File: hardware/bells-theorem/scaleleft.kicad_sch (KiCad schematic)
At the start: 30 parts, among them U20 TL074, U21 TL072

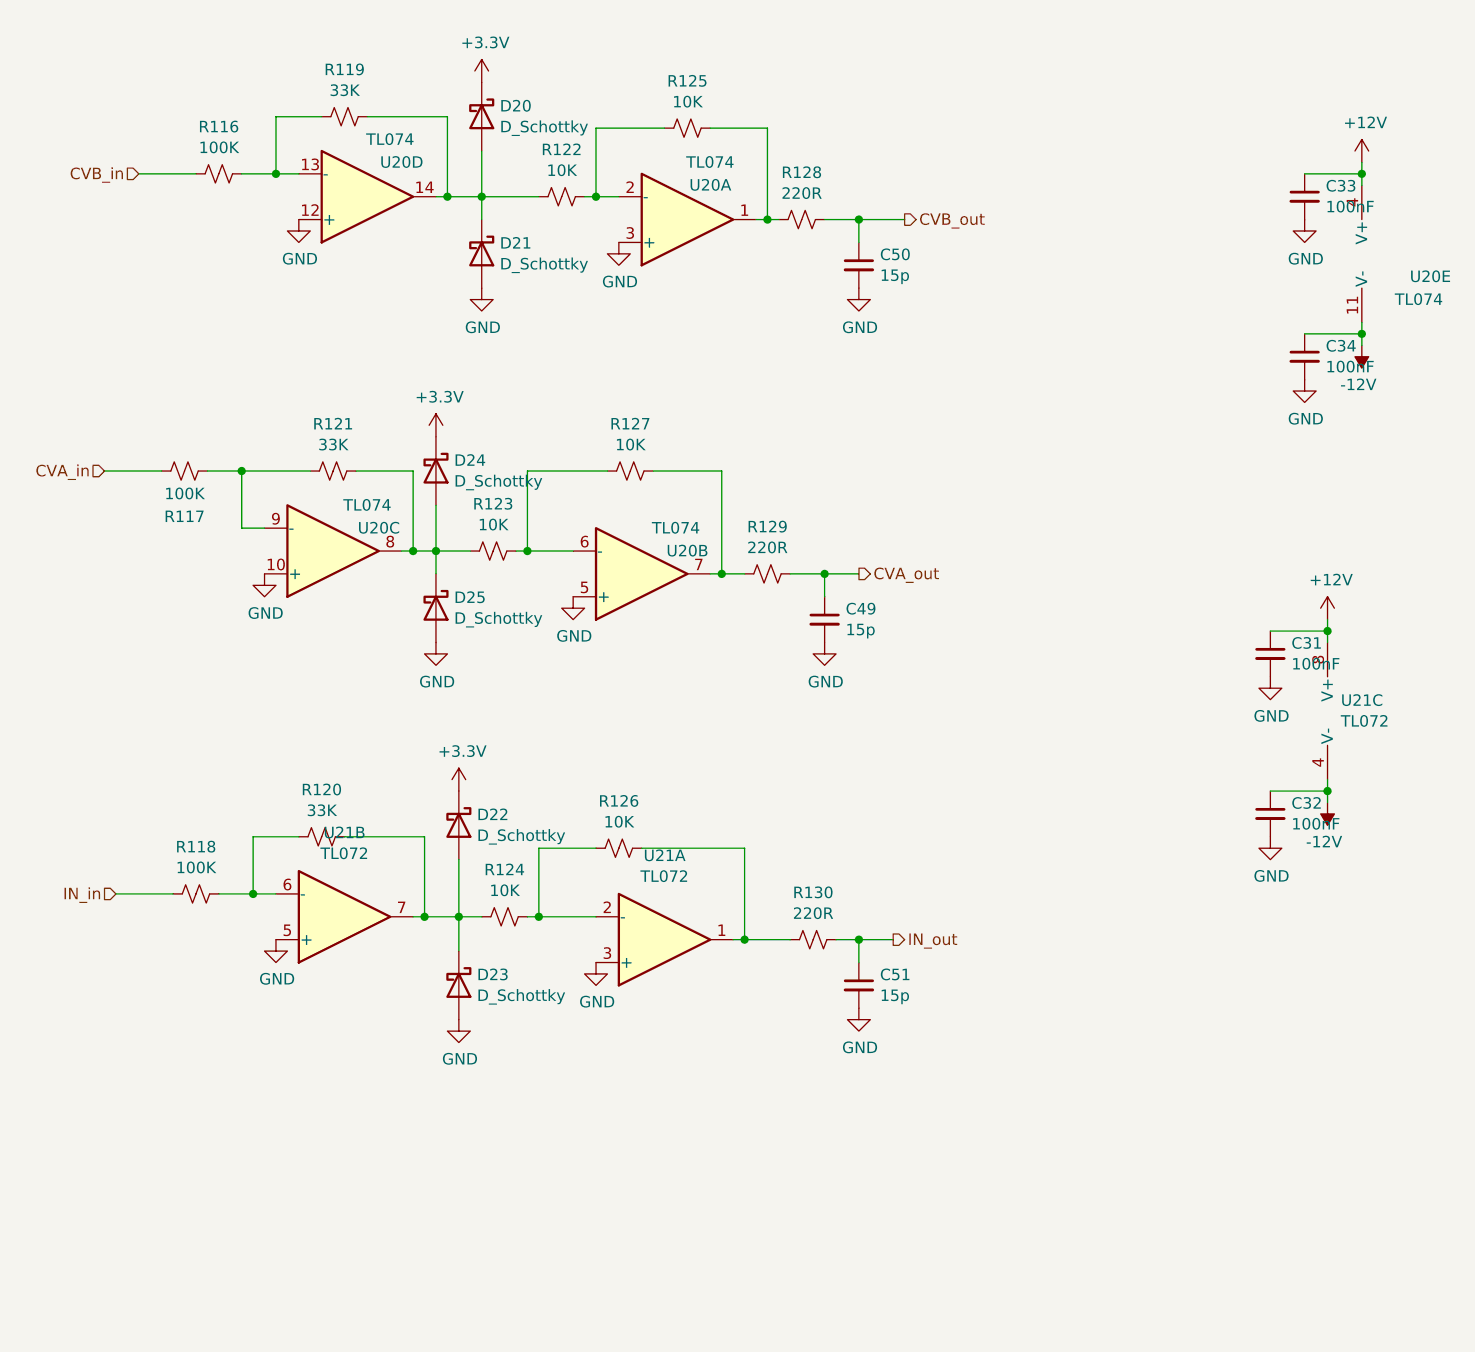
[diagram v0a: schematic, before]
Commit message: Modified with Jim M's recommendations for input scaling
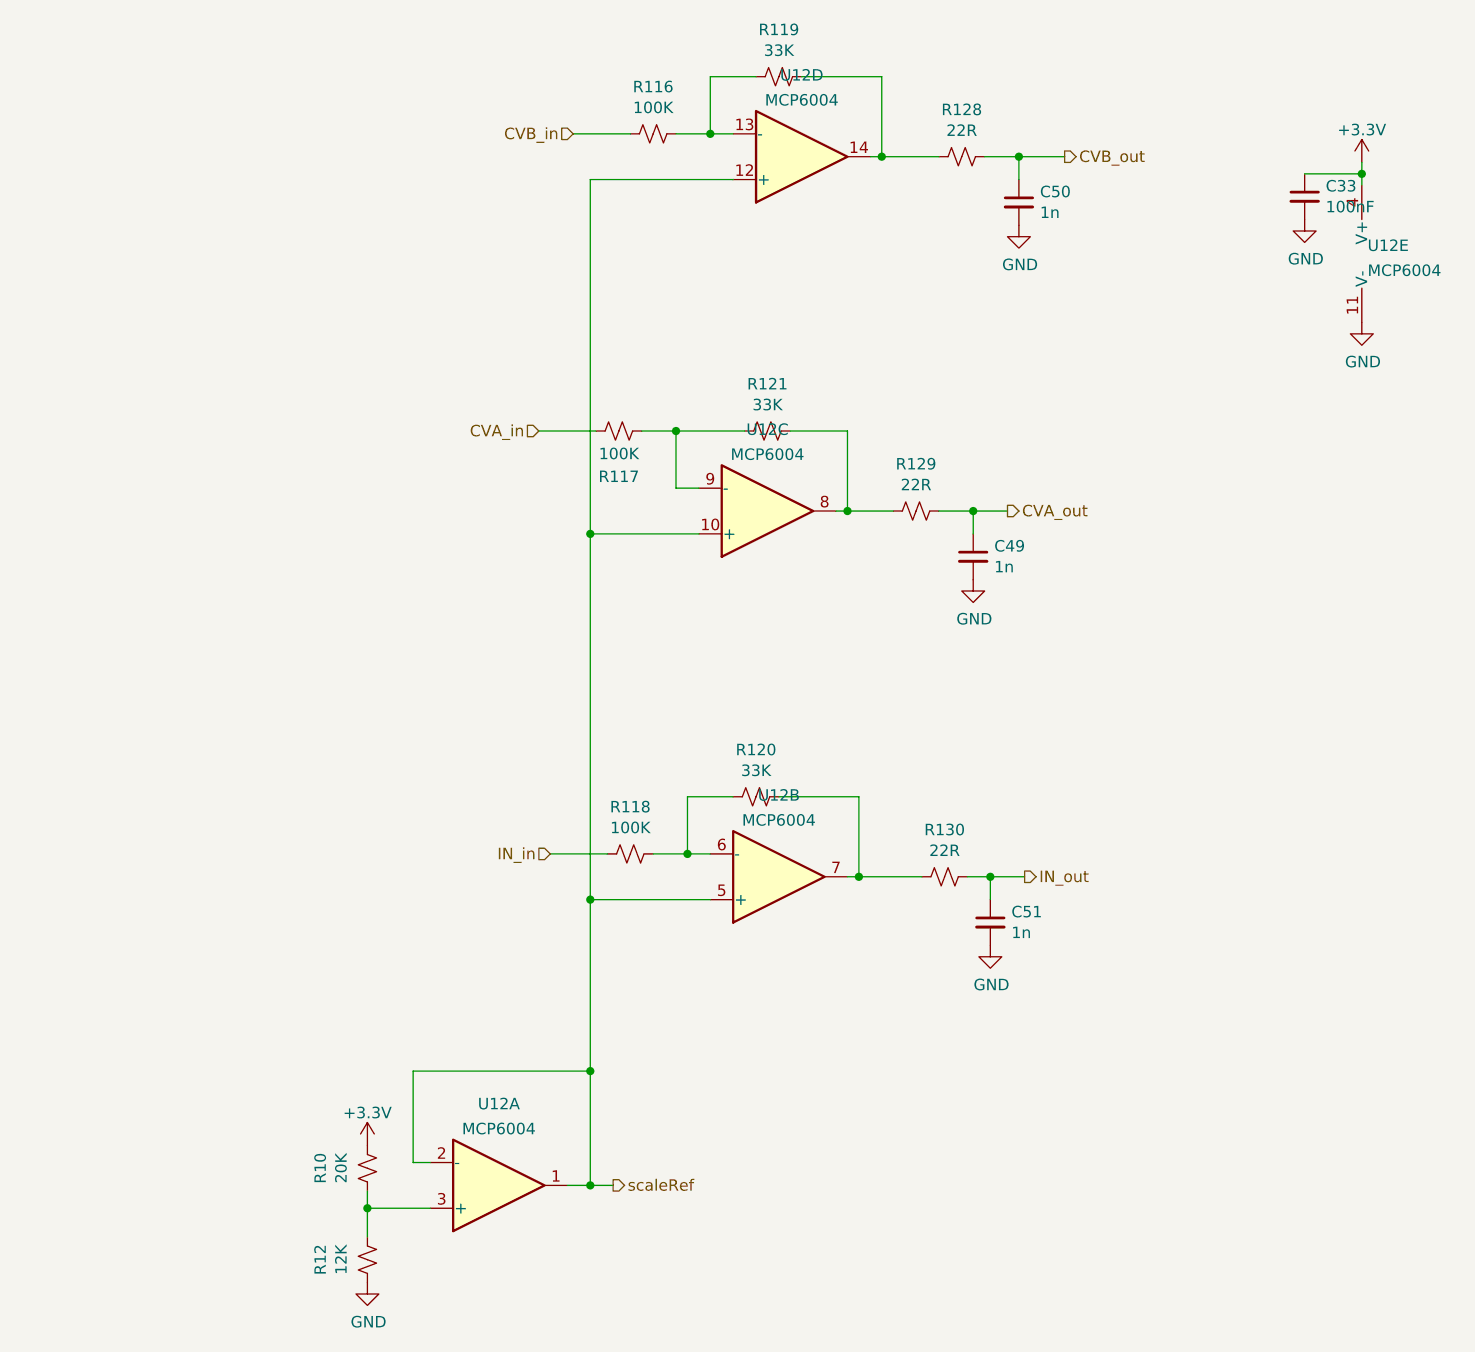
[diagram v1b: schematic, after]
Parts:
- removed C31, C32, C34: 100nF, Capacitor_SMD:C_0805_2012Metric_Pad1.15x1.40mm_HandSolder, symbol Device:C_Small
- removed D20, D21, D22, D23, D24, D25: D_Schottky, Resistor_SMD:R_0805_2012Metric_Pad1.15x1.40mm_HandSolder, symbol Device:D_Schottky
- removed R122, R123, R124, R125, R126, R127: 10K, Resistor_SMD:R_0805_2012Metric_Pad1.15x1.40mm_HandSolder, symbol Device:R_Small_US
- removed U20: TL074, Package_SO:SOIC-14_3.9x8.7mm_P1.27mm, symbol Amplifier_Operational:TL074
- removed U21: TL072, Package_SO:SOIC-8_3.9x4.9mm_P1.27mm, symbol Amplifier_Operational:TL072
- added R10: 20K, Resistor_SMD:R_0805_2012Metric_Pad1.15x1.40mm_HandSolder, symbol Device:R_Small_US
- added R12: 12K, Resistor_SMD:R_0805_2012Metric_Pad1.15x1.40mm_HandSolder, symbol Device:R_Small_US
- added U12: MCP6004, symbol Amplifier_Operational:MCP6004
- C49, C50, C51: value 15p -> 1n
- R128, R129, R130: value 220R -> 22R
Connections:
- net +12V is gone; now on net +3V3: C33.1
- net +3V3: now also R10.1, U12.4 (V+)
- net GND: now also R12.2, U12.11 (V-)
- net at R116.1, R119.2: now also U12.13 (-)
- net at R119.1: now also R128.2, U12.14
- net at R121.1: now also R129.2, U12.8
- net at R117.1, R121.2: now also U12.9 (-)
- net at R118.1, R120.2: now also U12.6 (-)
- net at R120.1: now also R130.2, U12.7
- new net: R10.2, R12.1, U12.3 (+)
- new net scaleRef: U12.1, U12.10 (+), U12.12 (+), U12.2 (-), U12.5 (+)
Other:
- moved on the sheet: C49, C50, C51, R116, R117, R118, R119, R120, R121, R128, R129, R130

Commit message: All changes up to date with latest revisions
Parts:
- C33: footprint Capacitor_SMD:C_0805_2012Metric_Pad1.15x1.40mm_HandSolder -> Capacitor_SMD:C_0805_2012Metric_Pad1.18x1.45mm_HandSolder
- R10, R116, R117, R118, R119, R12, R120, R121, R128, R129, R130: footprint Resistor_SMD:R_0805_2012Metric_Pad1.15x1.40mm_HandSolder -> Resistor_SMD:R_0805_2012Metric_Pad1.20x1.40mm_HandSolder
- U12: footprint (none) -> Package_SO:SO-14_3.9x8.65mm_P1.27mm
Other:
- title: (none) -> Bell's Theorem
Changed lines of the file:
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@@
 (kicad_sch (version 20211123) (generator eeschema)
   (paper "A4")
+  (title_block
+    (title "Bell's Theorem")
+    (date "2022-01-16")
+  )
   (junction (at 139.7 79.375) (diameter 0) (color 0 0 0 0)
   )
@@
     (property "Reference" "R116" (id 0) (at 118.11 32.258 90))
     (property "Value" "100K" (id 1) (at 118.11 34.5694 90))
-    (property "Footprint" "Resistor_SMD:R_0805_2012Metric_Pad1.15x1.40mm_HandSolder" (id 2) (at 118.11 37.465 0)
+    (property "Footprint" "Resistor_SMD:R_0805_2012Metric_Pad1.20x1.40mm_HandSolder" (id 2) (at 118.11 37.465 0)
       (effects (font (size 1.27 1.27)) hide)
     )
@@
     (property "Reference" "R117" (id 0) (at 114.3 75.565 90))
     (property "Value" "100K" (id 1) (at 114.3 73.025 90))
-    (property "Footprint" "Resistor_SMD:R_0805_2012Metric_Pad1.15x1.40mm_HandSolder" (id 2) (at 114.3 70.485 0)
+    (property "Footprint" "Resistor_SMD:R_0805_2012Metric_Pad1.20x1.40mm_HandSolder" (id 2) (at 114.3 70.485 0)
       (effects (font (size 1.27 1.27)) hide)
     )
@@
     (property "Reference" "R119" (id 0) (at 132.08 25.908 90))
     (property "Value" "33K" (id 1) (at 132.08 28.2194 90))
-    (property "Footprint" "Resistor_SMD:R_0805_2012Metric_Pad1.15x1.40mm_HandSolder" (id 2) (at 132.08 31.115 0)
+    (property "Footprint" "Resistor_SMD:R_0805_2012Metric_Pad1.20x1.40mm_HandSolder" (id 2) (at 132.08 31.115 0)
       (effects (font (size 1.27 1.27)) hide)
     )
@@
     (property "Reference" "R121" (id 0) (at 130.81 65.278 90))
     (property "Value" "33K" (id 1) (at 130.81 67.5894 90))
-    (property "Footprint" "Resistor_SMD:R_0805_2012Metric_Pad1.15x1.40mm_HandSolder" (id 2) (at 130.81 70.485 0)
+    (property "Footprint" "Resistor_SMD:R_0805_2012Metric_Pad1.20x1.40mm_HandSolder" (id 2) (at 130.81 70.485 0)
       (effects (font (size 1.27 1.27)) hide)
     )
@@
     (property "Reference" "R129" (id 0) (at 147.32 74.168 90))
     (property "Value" "22R" (id 1) (at 147.32 76.4794 90))
-    (property "Footprint" "Resistor_SMD:R_0805_2012Metric_Pad1.15x1.40mm_HandSolder" (id 2) (at 147.32 79.375 0)
+    (property "Footprint" "Resistor_SMD:R_0805_2012Metric_Pad1.20x1.40mm_HandSolder" (id 2) (at 147.32 79.375 0)
       (effects (font (size 1.27 1.27)) hide)
     )
@@
     (property "Reference" "R128" (id 0) (at 152.4 34.798 90))
     (property "Value" "22R" (id 1) (at 152.4 37.1094 90))
-    (property "Footprint" "Resistor_SMD:R_0805_2012Metric_Pad1.15x1.40mm_HandSolder" (id 2) (at 152.4 40.005 0)
+    (property "Footprint" "Resistor_SMD:R_0805_2012Metric_Pad1.20x1.40mm_HandSolder" (id 2) (at 152.4 40.005 0)
       (effects (font (size 1.27 1.27)) hide)
     )
@@
     (property "Reference" "R118" (id 0) (at 115.57 112.268 90))
     (property "Value" "100K" (id 1) (at 115.57 114.5794 90))
-    (property "Footprint" "Resistor_SMD:R_0805_2012Metric_Pad1.15x1.40mm_HandSolder" (id 2) (at 115.57 117.475 0)
+    (property "Footprint" "Resistor_SMD:R_0805_2012Metric_Pad1.20x1.40mm_HandSolder" (id 2) (at 115.57 117.475 0)
       (effects (font (size 1.27 1.27)) hide)
     )
@@
     (property "Reference" "R120" (id 0) (at 129.54 105.918 90))
     (property "Value" "33K" (id 1) (at 129.54 108.2294 90))
-    (property "Footprint" "Resistor_SMD:R_0805_2012Metric_Pad1.15x1.40mm_HandSolder" (id 2) (at 129.54 111.125 0)
+    (property "Footprint" "Resistor_SMD:R_0805_2012Metric_Pad1.20x1.40mm_HandSolder" (id 2) (at 129.54 111.125 0)
       (effects (font (size 1.27 1.27)) hide)
     )
@@
     (property "Reference" "R130" (id 0) (at 150.495 114.808 90))
     (property "Value" "22R" (id 1) (at 150.495 117.1194 90))
-    (property "Footprint" "Resistor_SMD:R_0805_2012Metric_Pad1.15x1.40mm_HandSolder" (id 2) (at 150.495 120.015 0)
+    (property "Footprint" "Resistor_SMD:R_0805_2012Metric_Pad1.20x1.40mm_HandSolder" (id 2) (at 150.495 120.015 0)
       (effects (font (size 1.27 1.27)) hide)
     )
@@
       (effects (font (size 1.27 1.27)) (justify left))
     )
-    (property "Footprint" "Capacitor_SMD:C_0805_2012Metric_Pad1.15x1.40mm_HandSolder" (id 2) (at 190.5 44.45 0)
+    (property "Footprint" "Capacitor_SMD:C_0805_2012Metric_Pad1.18x1.45mm_HandSolder" (id 2) (at 190.5 44.45 0)
       (effects (font (size 1.27 1.27)) hide)
     )
@@
     (property "Reference" "U12" (id 0) (at 100.965 145.2585 0))
     (property "Value" "MCP6004" (id 1) (at 100.965 148.0336 0))
-    (property "Footprint" "" (id 2) (at 99.695 156.845 0)
+    (property "Footprint" "Package_SO:SO-14_3.9x8.65mm_P1.27mm" (id 2) (at 99.695 156.845 0)
       (effects (font (size 1.27 1.27)) hide)
     )
@@
     (property "Reference" "U12" (id 0) (at 134.62 30.9585 0))
     (property "Value" "MCP6004" (id 1) (at 134.62 33.7336 0))
-    (property "Footprint" "" (id 2) (at 133.35 42.545 0)
+    (property "Footprint" "Package_SO:SO-14_3.9x8.65mm_P1.27mm" (id 2) (at 133.35 42.545 0)
       (effects (font (size 1.27 1.27)) hide)
     )
@@
     (property "Reference" "R10" (id 0) (at 81.153 152.4 90))
     (property "Value" "20K" (id 1) (at 83.4644 152.4 90))
-    (property "Footprint" "Resistor_SMD:R_0805_2012Metric_Pad1.15x1.40mm_HandSolder" (id 2) (at 86.36 152.4 0)
+    (property "Footprint" "Resistor_SMD:R_0805_2012Metric_Pad1.20x1.40mm_HandSolder" (id 2) (at 86.36 152.4 0)
       (effects (font (size 1.27 1.27)) hide)
     )
@@
     (property "Reference" "R12" (id 0) (at 81.153 162.56 90))
     (property "Value" "12K" (id 1) (at 83.4644 162.56 90))
-    (property "Footprint" "Resistor_SMD:R_0805_2012Metric_Pad1.15x1.40mm_HandSolder" (id 2) (at 86.36 162.56 0)
+    (property "Footprint" "Resistor_SMD:R_0805_2012Metric_Pad1.20x1.40mm_HandSolder" (id 2) (at 86.36 162.56 0)
       (effects (font (size 1.27 1.27)) hide)
     )
@@
     (property "Reference" "U12" (id 0) (at 130.81 70.3285 0))
     (property "Value" "MCP6004" (id 1) (at 130.81 73.1036 0))
-    (property "Footprint" "" (id 2) (at 129.54 81.915 0)
+    (property "Footprint" "Package_SO:SO-14_3.9x8.65mm_P1.27mm" (id 2) (at 129.54 81.915 0)
       (effects (font (size 1.27 1.27)) hide)
     )
@@
       (effects (font (size 1.27 1.27)) (justify left))
     )
-    (property "Footprint" "" (id 2) (at 198.12 48.26 0)
+    (property "Footprint" "Package_SO:SO-14_3.9x8.65mm_P1.27mm" (id 2) (at 198.12 48.26 0)
       (effects (font (size 1.27 1.27)) hide)
     )
@@
     (property "Reference" "U12" (id 0) (at 132.08 110.9685 0))
     (property "Value" "MCP6004" (id 1) (at 132.08 113.7436 0))
-    (property "Footprint" "" (id 2) (at 130.81 122.555 0)
-      (effects (font (size 1.27 1.27)) hide)
-    )
+    (property "Footprint" "Package_SO:SO-14_3.9x8.65mm_P1.27mm" (id 2) (at 130.81 122.555 0)
+      (effects (font (size 1.27 1.27)) hide)
+    )

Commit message: last hardware / software updates
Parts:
- R119, R121: value 33K -> 47K
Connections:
- net GND: now also R119.2, R121.2
- net at R128.2, U12.14: now also U12.13 (-); no longer R119.1
- net at R129.2, U12.8: now also U12.9 (-); no longer R121.1
- net at R118.1, U12.6 (-): now also R120.1; no longer R120.2
- net at R130.2, U12.7: now also R120.2; no longer R120.1
- net scaleRef: no longer names the net of U12.1, U12.2 (-), U12.5 (+)
- net scaleRef: no longer U12.10 (+), U12.12 (+)
- new net: R116.1, R119.1, U12.12 (+)
- new net: R117.1, R121.1, U12.10 (+)
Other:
- note added: "INCORRECT"
- moved on the sheet: C33, C49, C50, C51, R10, R116, R117, R118, R119, R12, R120, R121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
